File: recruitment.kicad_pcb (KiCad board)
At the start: 2 copper layers, 1 part

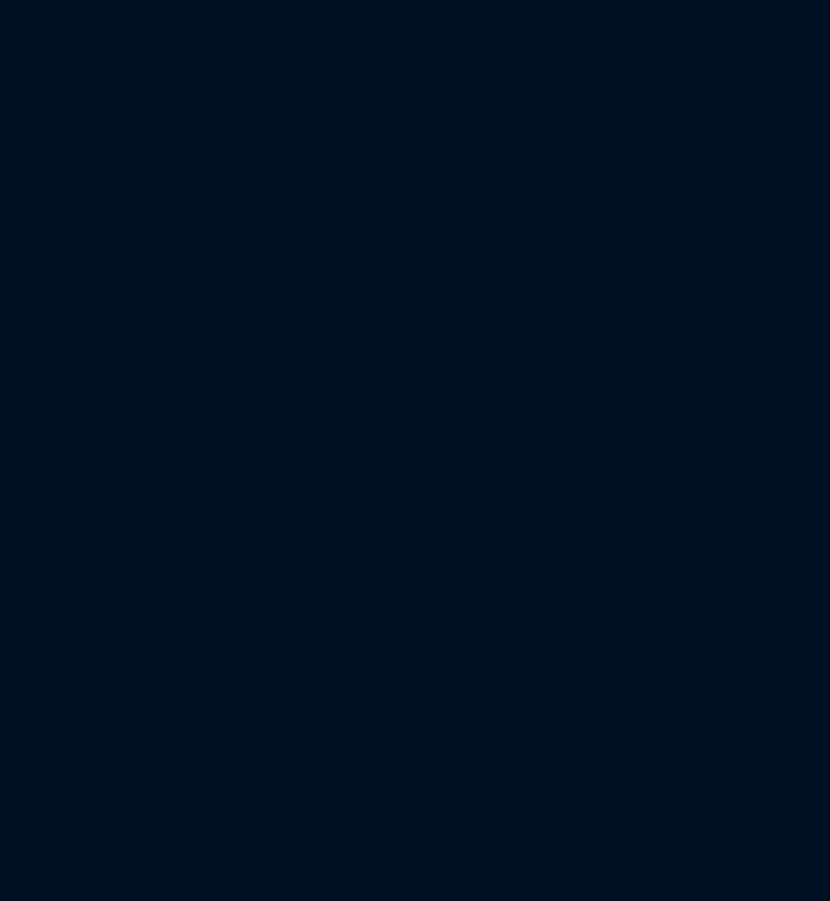
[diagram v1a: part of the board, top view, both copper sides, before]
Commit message: Safety update
Updating not to loose work
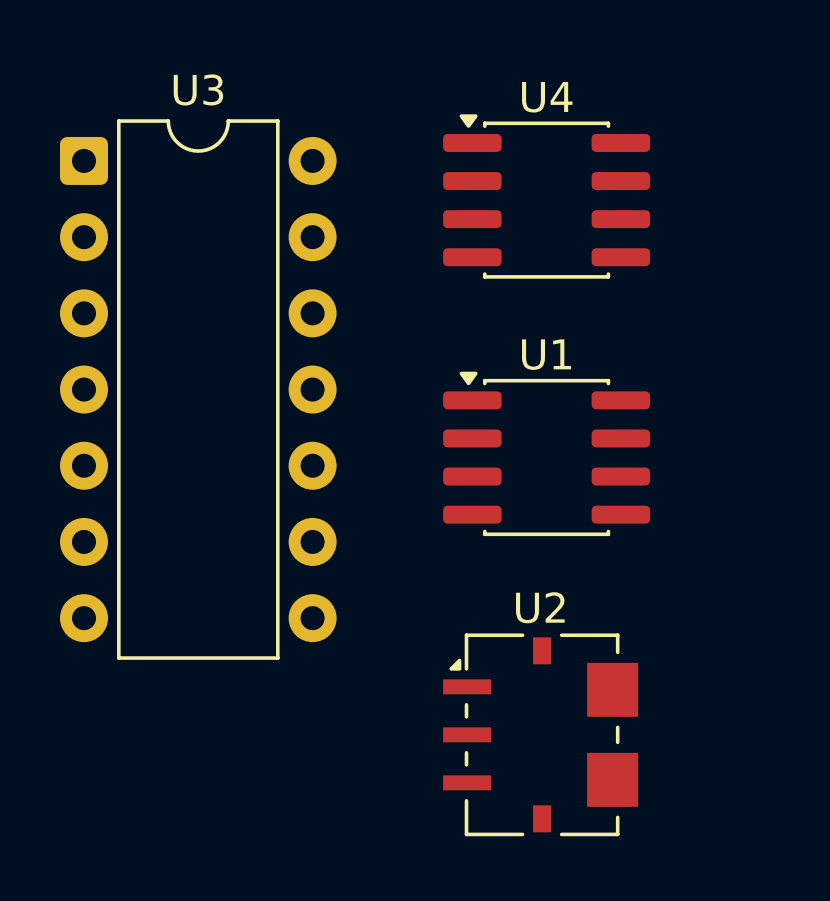
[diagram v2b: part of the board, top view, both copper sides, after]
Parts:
- added U1: XL1509-12, Package_SO:SOIC-8_3.9x4.9mm_P1.27mm, F.Cu at (115.8, 76.8)
- added U2: ACS781xLRTR-050B, Sensor_Current:Allegro_PSOF-7_4.8x6.4mm_P1.60mm, F.Cu at (115.6, 86.0)
- added U3: MPY634KP, Package_DIP:DIP-14_W7.62mm, F.Cu at (100.4, 66.9)
- added U4: NE555D, Package_SO:SOIC-8_3.9x4.9mm_P1.27mm, F.Cu at (115.8, 68.2)

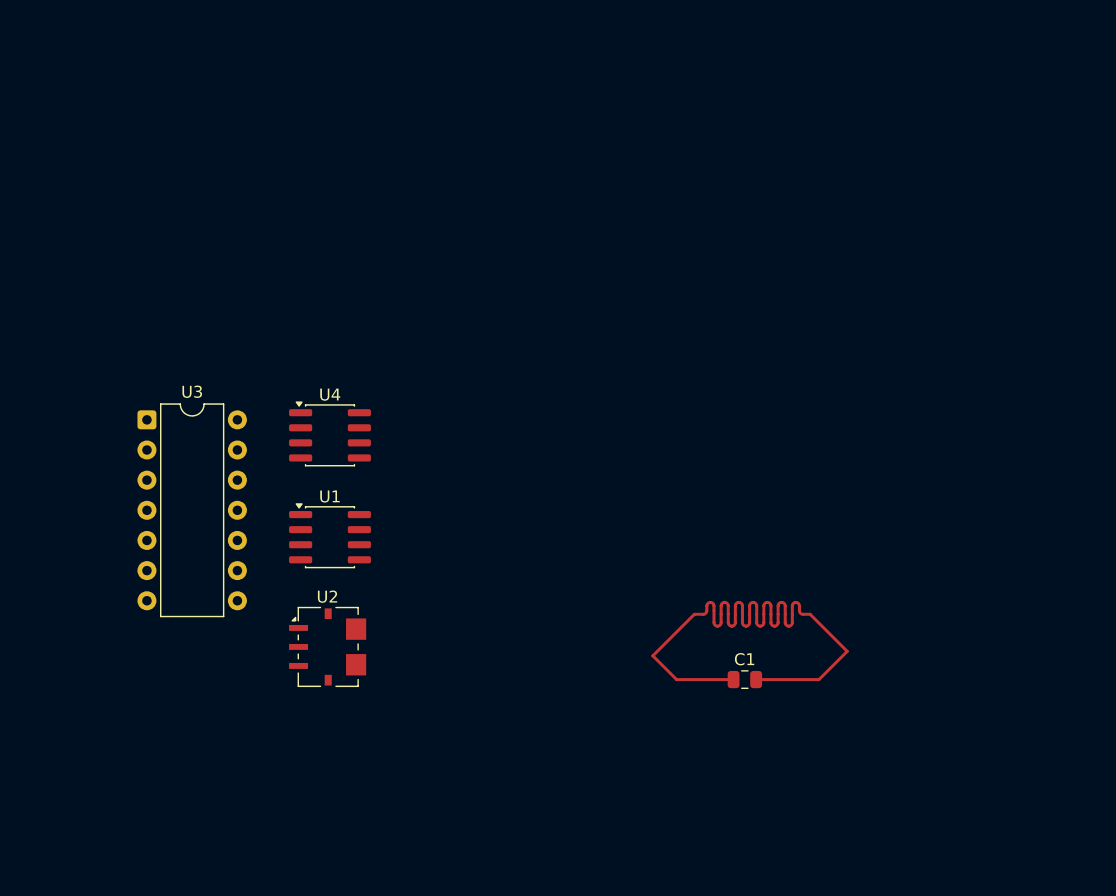
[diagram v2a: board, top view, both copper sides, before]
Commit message: Finished (?)
Assigned al values, footprints and generated traces.
Generated DRL files.
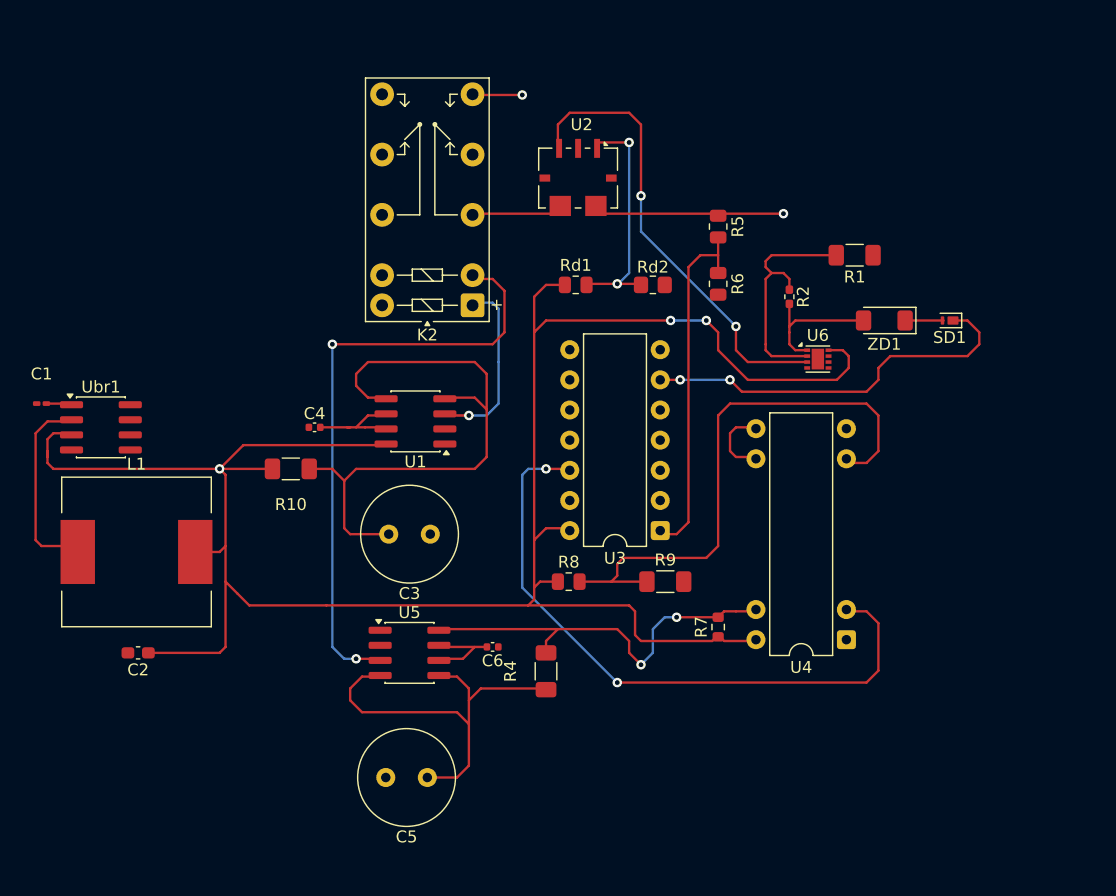
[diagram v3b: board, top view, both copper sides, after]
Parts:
- added C2: C (180microF), Capacitor_SMD:C_0603_1608Metric_Pad1.08x0.95mm_HandSolder, F.Cu at (99.6, 86.5)
- added C3: 100 uF, Capacitor_THT:C_Radial_D8.0mm_H7.0mm_P3.50mm, F.Cu at (124.2, 76.5)
- added C4: 10 nF, Capacitor_SMD:C_0402_1005Metric, F.Cu at (114.5, 67.5)
- added C5: 100 uF, Capacitor_THT:C_Radial_D8.0mm_H7.0mm_P3.50mm, F.Cu at (120.5, 97.0)
- added C6: 10 nF, Capacitor_SMD:C_0402_1005Metric, F.Cu at (129.5, 86.0)
- added K2: G6AK, Relay_THT:Relay_DPDT_Omron_G6AK, F.Cu at (127.8, 57.2)
- added L1: L (68 microH-2A), Inductor_SMD:L_12x12mm_H8mm, F.Cu at (99.5, 78.0)
- added R1: 1 kOhm, Resistor_SMD:R_1206_3216Metric_Pad1.30x1.75mm_HandSolder, F.Cu at (160.0, 53.0)
- added R10: 100 kOhm, Resistor_SMD:R_1206_3216Metric_Pad1.30x1.75mm_HandSolder, F.Cu at (112.5, 71.0)
- added R2: 2 kOhm, Resistor_SMD:R_0402_1005Metric_Pad0.72x0.64mm_HandSolder, F.Cu at (154.5, 56.5)
- added R4: 100 kOhm, Resistor_SMD:R_1206_3216Metric_Pad1.30x1.75mm_HandSolder, F.Cu at (134.0, 88.0)
- added R5: 125 kOhm, Resistor_SMD:R_0805_2012Metric, F.Cu at (148.5, 50.6)
- added R6: 25 kOhm, Resistor_SMD:R_0805_2012Metric, F.Cu at (148.5, 55.4)
- added R7: 20 kOhm, Resistor_SMD:R_0603_1608Metric, F.Cu at (148.5, 84.3)
- added R8: 1.4 kOhm, Resistor_SMD:R_0805_2012Metric, F.Cu at (135.9, 80.5)
- added R9: 1 kOhm, Resistor_SMD:R_1206_3216Metric_Pad1.30x1.75mm_HandSolder, F.Cu at (144.1, 80.5)
- added Rd1: 791 Ohm, Resistor_SMD:R_0805_2012Metric, F.Cu at (136.5, 55.5)
- added Rd2: 300 Ohm, Resistor_SMD:R_0805_2012Metric_Pad1.20x1.40mm_HandSolder, F.Cu at (143.0, 55.5)
- added SD1: 0.2V VDrop, Diode_SMD:Nexperia_DSN1608-2_1.6x0.8mm, F.Cu at (168.0, 58.5)
- added U5: NE555D, Package_SO:SOIC-8_3.9x4.9mm_P1.27mm, F.Cu at (122.5, 86.5)
- added U6: LM358_DFN, Package_DFN_QFN:DFN-8-1EP_2x2mm_P0.5mm_EP1.05x1.75mm, F.Cu at (156.9, 61.8)
- added Ubr1: XL1509-12, Package_SO:SOIC-8_3.9x4.9mm_P1.27mm, F.Cu at (96.5, 67.5)
- added ZD1: 4.7 VDrop ZD, Diode_SMD:D_MiniMELF, F.Cu at (162.5, 58.5)
- C1: value 1F -> 550 microF; footprint Capacitor_SMD:C_0805_2012Metric -> Capacitor_SMD:C_0201_0603Metric_Pad0.64x0.40mm_HandSolder
- U1: value XL1509-12 -> NE555D
- U4: value NE555D -> LM311; footprint Package_SO:SOIC-8_3.9x4.9mm_P1.27mm -> Package_DIP:DIP-8-16_W7.62mm
- moved C1 63.6 mm to (91.5, 65.5), turned to 180 degrees
- moved U4 46.8 mm to (159.3, 85.4), turned to 180 degrees
- moved U2 44.8 mm to (136.7, 46.5), turned to -90 degrees
- moved U3 44.2 mm to (143.6, 76.2), turned to 180 degrees
- moved U1 12.1 mm to (123.0, 67.0), turned to 180 degrees
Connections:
- C1 pad 1: Net-(C1-Pad1) -> Monitor Supply
- C1 pad 2: Net-(C1-Pad1) -> GND
- U1 pad 1: Monitor Supply -> GND
- U1 pad 2: Net-(U1-OUT) -> unconnected-(U1-TR-Pad2)
- U1 pad 3: /Buck Regulator/12V -> /555 One Shot Open/Vout
- U1 pad 4: LOAD -> Net-(U1-CV)
- U1 pad 5: LOAD -> Net-(U1-CV)
- U1 pad 6: LOAD -> Net-(U1-DIS)
- U1 pad 7: LOAD -> Net-(U1-DIS)
- U1 pad 8: LOAD -> /555 One Shot Open/Vin
- U2 pad 2: LOAD -> GND
- U2 pad 3: /Multiplier/INcurr -> /INcurrent correction/HSvoltage
- U2 pad 4: LOAD -> GND
- U2 pad 6: LOAD -> /Voltage and Current measuring/I OUT
- U2 pad 7: LOAD -> GND
- U3 pad 1: /Multiplier/INvolt -> /Multiplier and Comparator/INvolt
- U3 pad 10: LOAD -> GND
- U3 pad 11: unconnected-(U3-Z_{1}-Pad11) -> GND
- U3 pad 12: /Multiplier/Vout -> Net-(U3-V_{O})
- U3 pad 14: /Multiplier/Vs -> /Buck Regulator/12V
- U3 pad 2: LOAD -> GND
- U3 pad 6: /Multiplier/INcurr -> /INcurrent correction/Vout
- U3 pad 7: LOAD -> GND
- U3 pad 8: LOAD -> GND
- U4 pad 1: LOAD -> GND
- U4 pad 2: unconnected-(U4-TR-Pad2) -> Net-(U3-V_{O})
- U4 pad 3: /555 One Shot/Vout -> /Multiplier and Comparator/5V
- U4 pad 4: Net-(U4-CV) -> GND
- U4 pad 5: Net-(U4-CV) -> Net-(U4-BAL)
- U4 pad 6: Net-(U4-DIS) -> Net-(U4-BAL)
- U4 pad 7: Net-(U4-DIS) -> /555 One Shot Close/Vin
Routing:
- net Net-(C1-Pad1): track 57.5 -> 0.00 mm
- net Net-(U3-V_{O}): vias 0 -> 2
- net Net-(K2-Pad14): vias 0 -> 1
- net /Voltage and Current measuring/I OUT: vias 0 -> 1
- net /Voltage and Current measuring/3,3V: vias 0 -> 2
- net /INcurrent correction/Vout: vias 0 -> 2
- net /INcurrent correction/HSvoltage: vias 0 -> 2
- net /Buck Regulator/12V: vias 0 -> 1
- net /555 One Shot Open/Vout: vias 0 -> 1
- net /555 One Shot Close/Vout: vias 0 -> 2
- net /555 One Shot Close/Vin: vias 0 -> 2
- net (no net): vias 0 -> 2

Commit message: Updated Ground Plane
Added eccidentally removed ground plane for both top and bottom
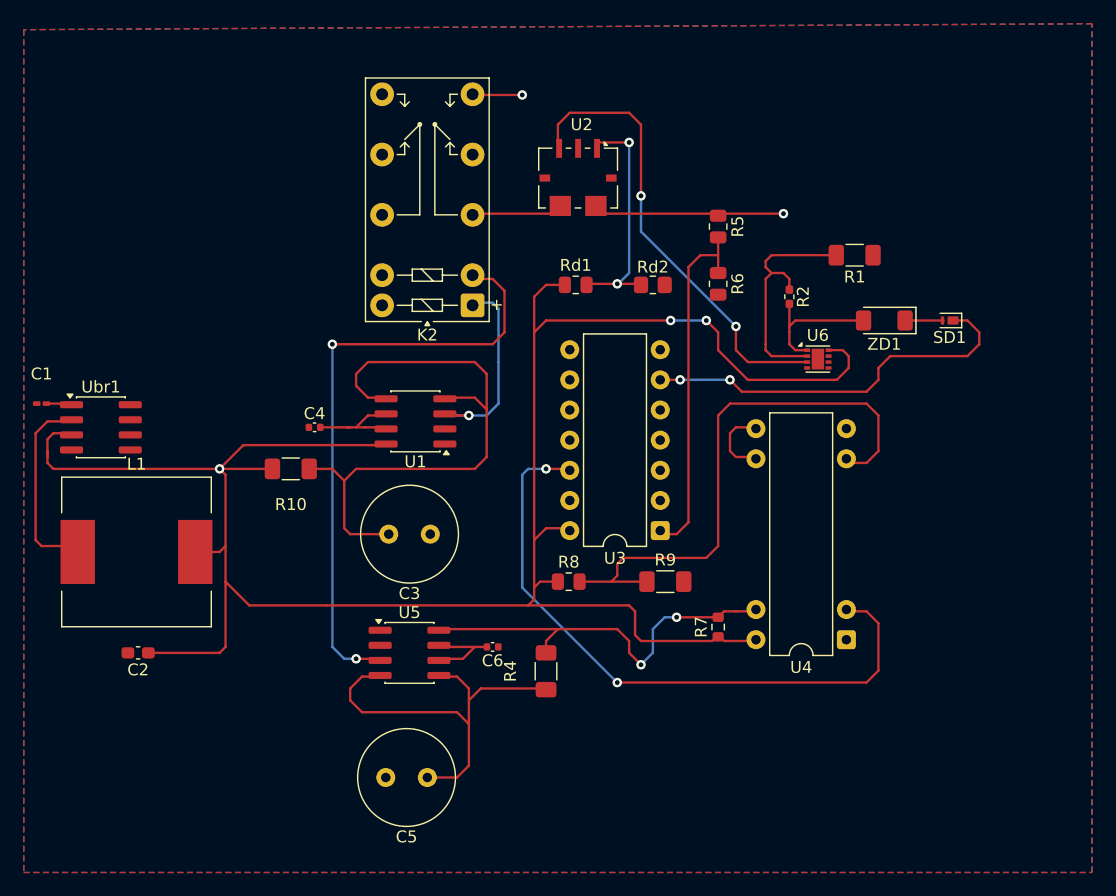
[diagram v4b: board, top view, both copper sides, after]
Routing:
- added copper zone on B.Cu, net GND
- added copper zone on F.Cu, net GND
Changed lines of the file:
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@@
 		(net 35)
+	)
+	(zone
+		(net 36)
+		(net_name "GND")
+		(layers "F.Cu" "B.Cu")
+		(hatch edge 0.5)
+		(connect_pads
+			(clearance 0.508)
+		)
+		(min_thickness 0.25)
+		(filled_areas_thickness no)
+		(fill yes
+			(thermal_gap 0.5)
+			(thermal_bridge_width 0.5)
+		)
+		(polygon
+			(pts
+				(xy 90 105) (xy 180 105) (xy 180 33.5) (xy 90 34)
+			)
+		)
 	)
 	(embedded_fonts no)
